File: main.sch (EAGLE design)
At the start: 49 parts, among them U2 SN65HVD32_D_8

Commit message: Organized Schematic
Added borders, boxes, and labels
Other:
- note added: "3.3V Switching Regulator"
- note added: "5V Tolerant Analog to Digital"
- note added: "BNO055 IMU"
- note added: "Designed around 100ohm output impedance pressure transducers"
- note added: "Digital IO Ports"
- note added: "Power Pins"
- note added: "RS-485 Tranceiver and Pins"
- note added: "SAMD21G18 Microcontroller"
- note added: "SWD Debuging Header"
- note added: "microSD card slot"
- note removed: "* MEANS UNFINISHED"
- note removed: "SAMD21G18"
- moved on the sheet: AIN, C1, C2, C23, C3, C4, C5, C6, C7, C8, C9, COM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

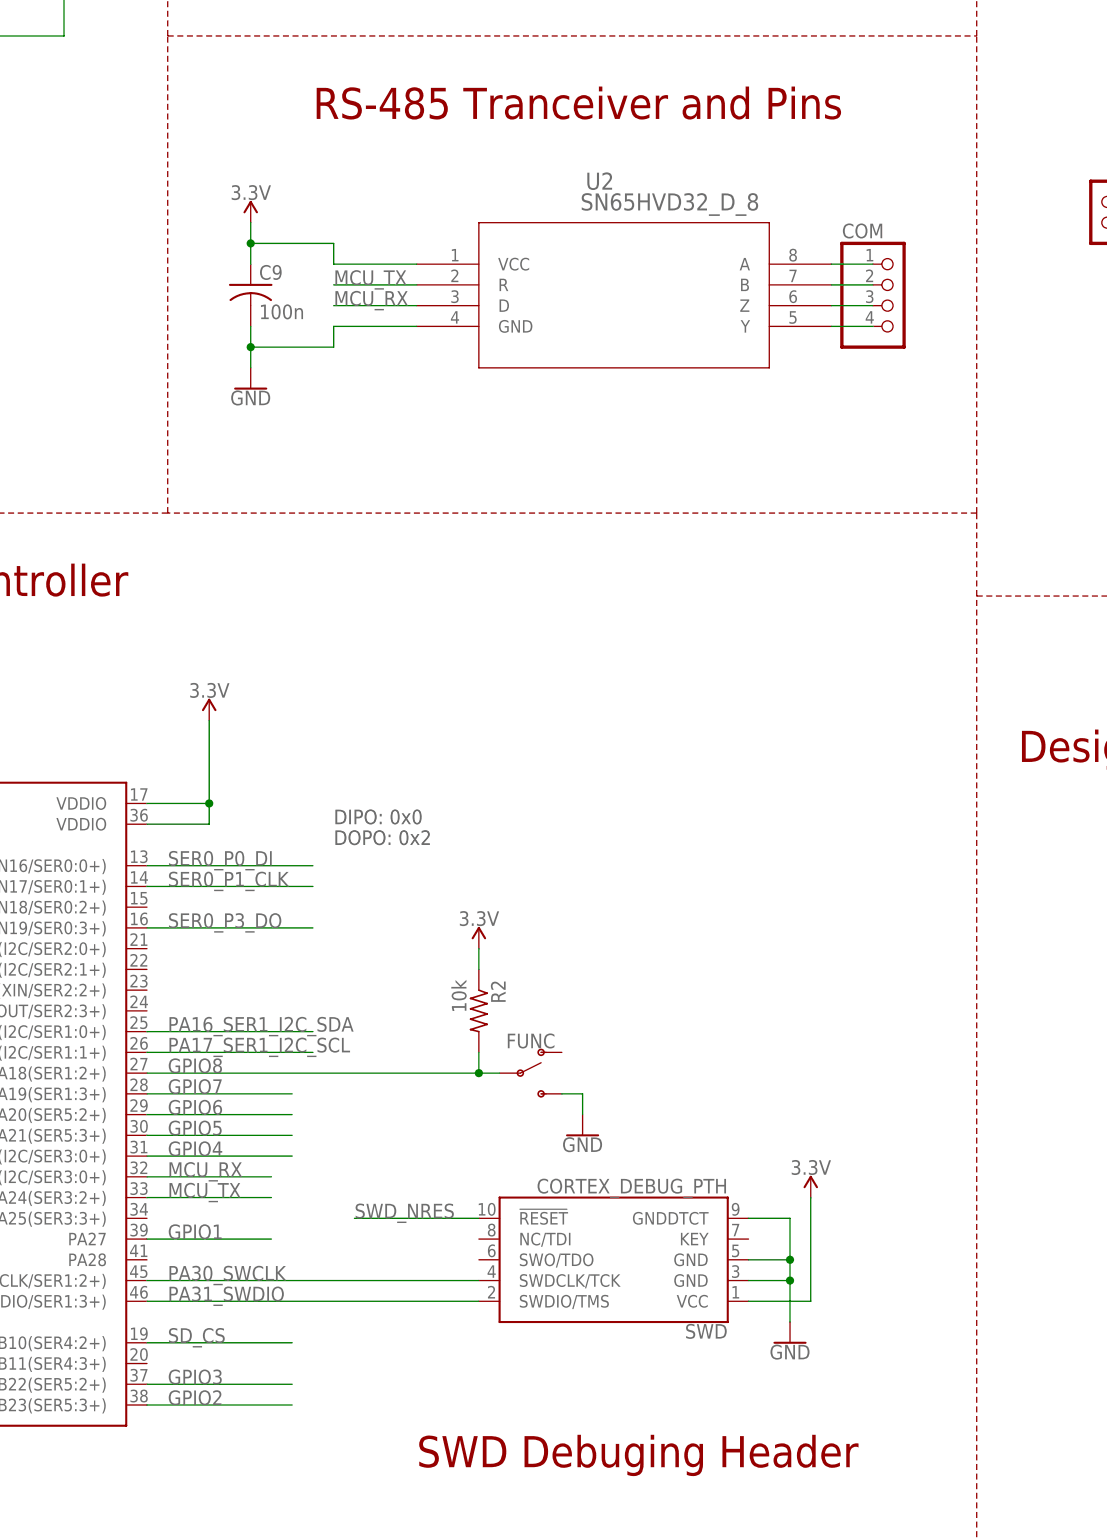
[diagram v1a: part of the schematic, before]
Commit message: Changed coms transceiver, and updated documentation
Also updated bill of materials
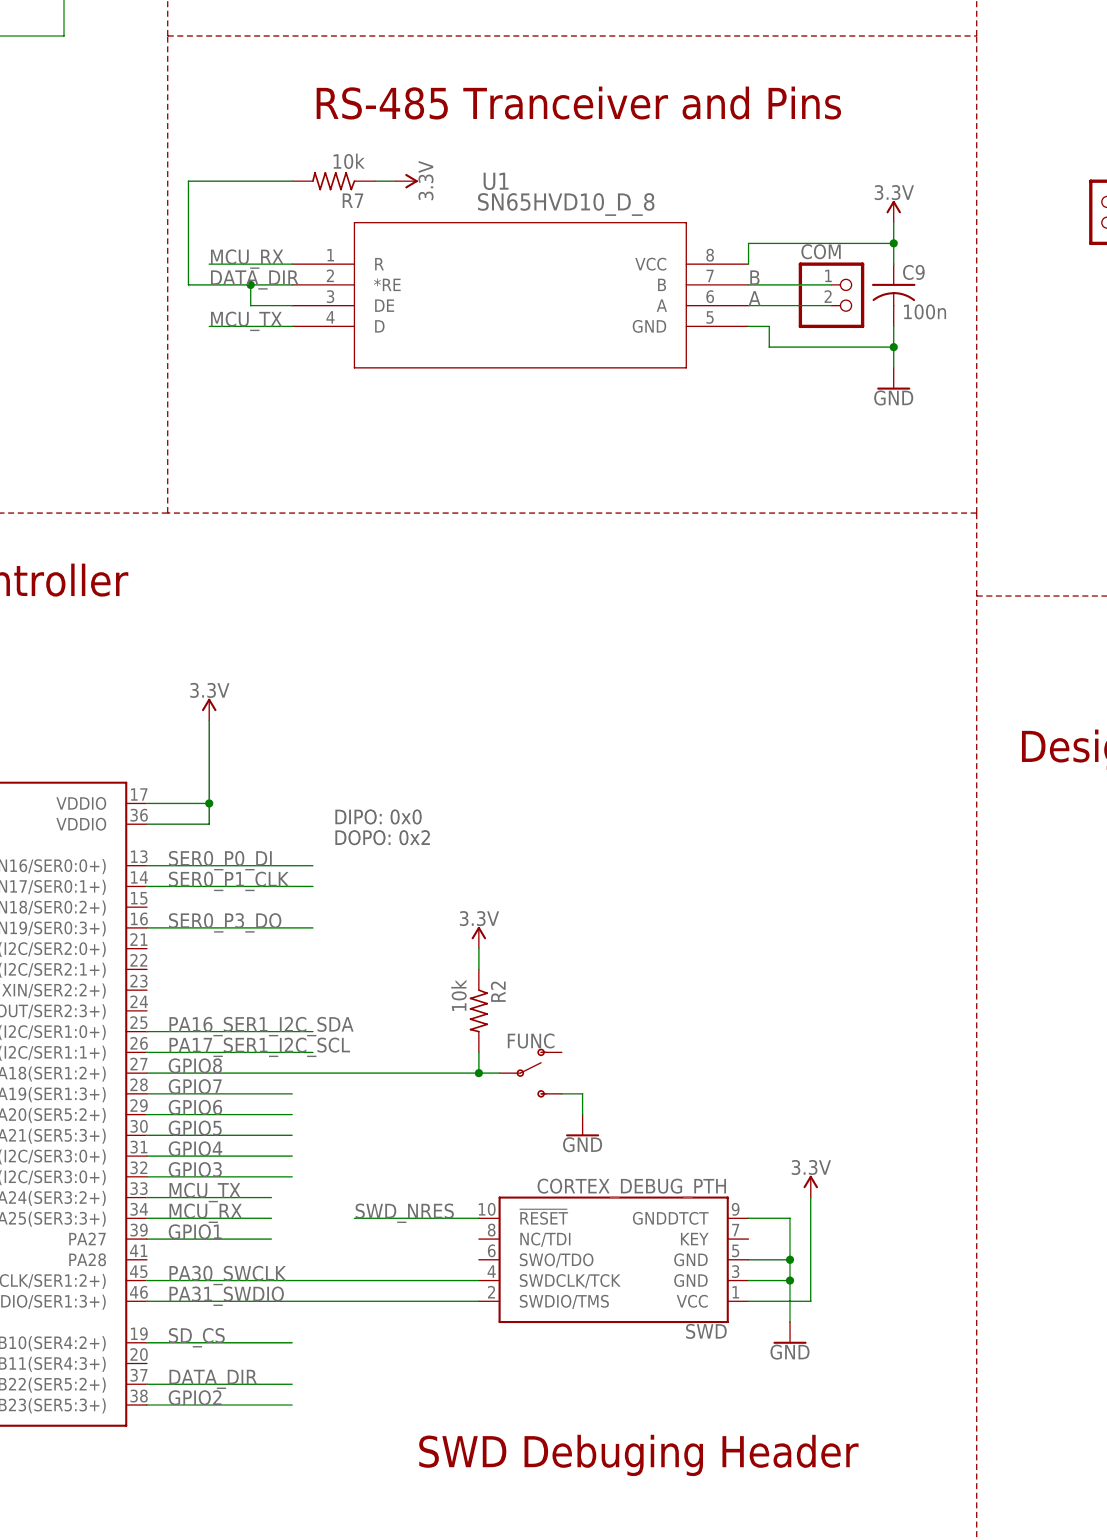
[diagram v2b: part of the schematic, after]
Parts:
- removed U2: SN65HVD32_D_8, SN65HVD32:SN65HVD32_D_8
- added R7: 10k, resistor:R-US_R0603
- added U1: SN65HVD10_D_8, half-dup-485:SN65HVD10_D_8
- COM: device pinhead:PINHD-1X4 -> pinhead:PINHD-1X2
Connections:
- removed net Y: COM.4, U2.Y
- removed net Z: COM.3, U2.Z
- new net DATA_DIR: MCU.PB22(SER5:2+), R7.2, U1.*RE, U1.DE
- net 3.3V: now also R7.1, U1.VCC; no longer U2.VCC
- net A: now also COM.2, U1.A; no longer COM.1, U2.A
- net B: now also COM.1, U1.B; no longer COM.2, U2.B
- net GND: now also U1.GND; no longer U2.GND
- net GPIO3: now also MCU.PA23(I2C/SER3:0+); no longer MCU.PB22(SER5:2+)
- net MCU_RX: now also MCU.PA25(SER3:3+), U1.R; no longer MCU.PA23(I2C/SER3:0+), U2.D
- net MCU_TX: now also U1.D; no longer U2.R
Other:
- moved on the sheet: C9
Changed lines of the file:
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@@
 <?xml version="1.0" encoding="utf-8"?>
 <!DOCTYPE eagle SYSTEM "eagle.dtd">
-<eagle version="8.6.3">
+<eagle version="8.6.0">
 <drawing>
 <settings>
@@
 <part name="SUPPLY16" library="SparkFun-PowerSymbols" deviceset="3.3V" device=""/>
 <part name="GND24" library="SparkFun-PowerSymbols" deviceset="GND" device=""/>
-<part name="U2" library="SN65HVD32" deviceset="SN65HVD32_D_8" device=""/>
-<part name="COM" library="pinhead" deviceset="PINHD-1X4" device=""/>
 <part name="AIN" library="pinhead" deviceset="PINHD-1X5" device=""/>
 <part name="VDUC" library="pinhead" deviceset="PINHD-1X2" device=""/>
@@
 <part name="PWR" library="SparkFun-Switches" deviceset="SWITCH-SPDT" device="-PTH-11.6X4.0MM"/>
 <part name="FRAME1" library="frames" library_urn="urn:adsk.eagle:library:229" deviceset="FRAME_B_L" device=""/>
+<part name="COM" library="pinhead" deviceset="PINHD-1X2" device=""/>
+<part name="U1" library="half-dup-485" deviceset="SN65HVD10_D_8" device=""/>
+<part name="R7" library="resistor" deviceset="R-US_" device="R0603" value="10k"/>
+<part name="SUPPLY13" library="SparkFun-PowerSymbols" deviceset="3.3V" device=""/>
 </parts>
 <sheets>
@@
 <instance part="R5" gate="G$1" x="76.2" y="109.22" rot="R270"/>
 <instance part="SUPPLY15" gate="G$1" x="76.2" y="116.84"/>
-<instance part="C9" gate="G$1" x="177.8" y="165.1"/>
-<instance part="SUPPLY16" gate="G$1" x="177.8" y="172.72"/>
-<instance part="GND24" gate="1" x="177.8" y="152.4"/>
-<instance part="U2" gate="A" x="198.12" y="167.64"/>
-<instance part="COM" gate="A" x="256.54" y="162.56"/>
+<instance part="C9" gate="G$1" x="256.54" y="165.1"/>
+<instance part="SUPPLY16" gate="G$1" x="256.54" y="172.72"/>
+<instance part="GND24" gate="1" x="256.54" y="152.4"/>
 <instance part="AIN" gate="A" x="393.7" y="91.44"/>
 <instance part="VDUC" gate="G$1" x="398.78" y="228.6"/>
@@
 <instance part="FRAME1" gate="G$1" x="0" y="0"/>
 <instance part="FRAME1" gate="G$2" x="325.12" y="0"/>
+<instance part="COM" gate="G$1" x="251.46" y="162.56"/>
+<instance part="U1" gate="A" x="182.88" y="167.64"/>
+<instance part="R7" gate="G$1" x="187.96" y="177.8" rot="R180"/>
+<instance part="SUPPLY13" gate="G$1" x="195.58" y="177.8" rot="R270"/>
 </instances>
 <busses>
@@
 <pinref part="C9" gate="G$1" pin="1"/>
 <pinref part="SUPPLY16" gate="G$1" pin="3.3V"/>
-<wire x1="177.8" y1="167.64" x2="177.8" y2="170.18" width="0.1524" layer="91"/>
-<pinref part="U2" gate="A" pin="VCC"/>
-<wire x1="177.8" y1="170.18" x2="177.8" y2="172.72" width="0.1524" layer="91"/>
-<wire x1="198.12" y1="167.64" x2="187.96" y2="167.64" width="0.1524" layer="91"/>
-<wire x1="187.96" y1="167.64" x2="187.96" y2="170.18" width="0.1524" layer="91"/>
-<wire x1="187.96" y1="170.18" x2="177.8" y2="170.18" width="0.1524" layer="91"/>
-<junction x="177.8" y="170.18"/>
+<wire x1="256.54" y1="167.64" x2="256.54" y2="170.18" width="0.1524" layer="91"/>
+<pinref part="U1" gate="A" pin="VCC"/>
+<wire x1="256.54" y1="170.18" x2="256.54" y2="172.72" width="0.1524" layer="91"/>
+<wire x1="238.76" y1="167.64" x2="238.76" y2="170.18" width="0.1524" layer="91"/>
+<wire x1="238.76" y1="170.18" x2="256.54" y2="170.18" width="0.1524" layer="91"/>
+<junction x="256.54" y="170.18"/>
 </segment>
 <segment>
@@
 <wire x1="205.74" y1="81.28" x2="205.74" y2="83.82" width="0.1524" layer="91"/>
 </segment>
+<segment>
+<pinref part="R7" gate="G$1" pin="1"/>
+<wire x1="193.04" y1="177.8" x2="195.58" y2="177.8" width="0.1524" layer="91"/>
+<pinref part="SUPPLY13" gate="G$1" pin="3.3V"/>
+</segment>
 </net>
 <net name="GND" class="0">
@@
 <pinref part="C9" gate="G$1" pin="2"/>
 <pinref part="GND24" gate="1" pin="GND"/>
-<wire x1="177.8" y1="154.94" x2="177.8" y2="157.48" width="0.1524" layer="91"/>
-<pinref part="U2" gate="A" pin="GND"/>
-<wire x1="177.8" y1="157.48" x2="177.8" y2="160.02" width="0.1524" layer="91"/>
-<wire x1="198.12" y1="160.02" x2="187.96" y2="160.02" width="0.1524" layer="91"/>
-<wire x1="187.96" y1="160.02" x2="187.96" y2="157.48" width="0.1524" layer="91"/>
-<wire x1="187.96" y1="157.48" x2="177.8" y2="157.48" width="0.1524" layer="91"/>
-<junction x="177.8" y="157.48"/>
+<wire x1="256.54" y1="154.94" x2="256.54" y2="157.48" width="0.1524" layer="91"/>
+<wire x1="256.54" y1="157.48" x2="256.54" y2="160.02" width="0.1524" layer="91"/>
+<wire x1="256.54" y1="157.48" x2="241.3" y2="157.48" width="0.1524" layer="91"/>
+<wire x1="241.3" y1="157.48" x2="241.3" y2="160.02" width="0.1524" layer="91"/>
+<junction x="256.54" y="157.48"/>
+<pinref part="U1" gate="A" pin="GND"/>
+<wire x1="241.3" y1="160.02" x2="238.76" y2="160.02" width="0.1524" layer="91"/>
 </segment>
 <segment>
@@
 <net name="MCU_TX" class="0">
 <segment>
-<pinref part="U2" gate="A" pin="R"/>
-<wire x1="198.12" y1="165.1" x2="187.96" y2="165.1" width="0.1524" layer="91"/>
-<label x="187.96" y="165.1" size="1.778" layer="95"/>
-</segment>
-<segment>
 <pinref part="MCU" gate="G$1" pin="PA24(SER3:2+)"/>
 <wire x1="165.1" y1="53.34" x2="180.34" y2="53.34" width="0.1524" layer="91"/>
 <label x="167.64" y="53.34" size="1.778" layer="95"/>
 </segment>
+<segment>
+<wire x1="182.88" y1="160.02" x2="172.72" y2="160.02" width="0.1524" layer="91"/>
+<label x="172.72" y="160.02" size="1.778" layer="95"/>
+<pinref part="U1" gate="A" pin="D"/>
+</segment>
 </net>
 <net name="MCU_RX" class="0">
 <segment>
-<pinref part="U2" gate="A" pin="D"/>
-<wire x1="198.12" y1="162.56" x2="187.96" y2="162.56" width="0.1524" layer="91"/>
-<label x="187.96" y="162.56" size="1.778" layer="95"/>
-</segment>
-<segment>
-<pinref part="MCU" gate="G$1" pin="PA23(I2C/SER3:0+)"/>
-<wire x1="165.1" y1="55.88" x2="180.34" y2="55.88" width="0.1524" layer="91"/>
-<label x="167.64" y="55.88" size="1.778" layer="95"/>
-</segment>
-</net>
-<net name="A" class="0">
-<segment>
-<pinref part="U2" gate="A" pin="A"/>
-<pinref part="COM" gate="A" pin="1"/>
-<wire x1="248.92" y1="167.64" x2="254" y2="167.64" width="0.1524" layer="91"/>
-</segment>
-</net>
-<net name="B" class="0">
-<segment>
-<pinref part="U2" gate="A" pin="B"/>
-<pinref part="COM" gate="A" pin="2"/>
-<wire x1="248.92" y1="165.1" x2="254" y2="165.1" width="0.1524" layer="91"/>
-</segment>
-</net>
-<net name="Z" class="0">
-<segment>
-<pinref part="U2" gate="A" pin="Z"/>
-<pinref part="COM" gate="A" pin="3"/>
-<wire x1="248.92" y1="162.56" x2="254" y2="162.56" width="0.1524" layer="91"/>
-</segment>
-</net>
-<net name="Y" class="0">
-<segment>
-<pinref part="U2" gate="A" pin="Y"/>
-<pinref part="COM" gate="A" pin="4"/>
-<wire x1="248.92" y1="160.02" x2="254" y2="160.02" width="0.1524" layer="91"/>
+<wire x1="182.88" y1="167.64" x2="172.72" y2="167.64" width="0.1524" layer="91"/>
+<label x="172.72" y="167.64" size="1.778" layer="95"/>
+<pinref part="U1" gate="A" pin="R"/>
+</segment>
+<segment>
+<pinref part="MCU" gate="G$1" pin="PA25(SER3:3+)"/>
+<wire x1="165.1" y1="50.8" x2="180.34" y2="50.8" width="0.1524" layer="91"/>
+<label x="167.64" y="50.8" size="1.778" layer="95"/>
 </segment>
 </net>
@@
 </segment>
 <segment>
-<pinref part="MCU" gate="G$1" pin="PB22(SER5:2+)"/>
-<wire x1="165.1" y1="30.48" x2="182.88" y2="30.48" width="0.1524" layer="91"/>
-<label x="167.64" y="30.48" size="1.778" layer="95"/>
+<pinref part="MCU" gate="G$1" pin="PA23(I2C/SER3:0+)"/>
+<wire x1="165.1" y1="55.88" x2="182.88" y2="55.88" width="0.1524" layer="91"/>
+<label x="167.64" y="55.88" size="1.778" layer="95"/>
 </segment>
 </net>
@@
 </segment>
 </net>
+<net name="DATA_DIR" class="0">
+<segment>
+<pinref part="U1" gate="A" pin="DE"/>
+<wire x1="182.88" y1="162.56" x2="177.8" y2="162.56" width="0.1524" layer="91"/>
+<wire x1="177.8" y1="162.56" x2="177.8" y2="165.1" width="0.1524" layer="91"/>
+<pinref part="U1" gate="A" pin="*RE"/>
+<wire x1="177.8" y1="165.1" x2="182.88" y2="165.1" width="0.1524" layer="91"/>
+<wire x1="177.8" y1="165.1" x2="170.18" y2="165.1" width="0.1524" layer="91"/>
+<junction x="177.8" y="165.1"/>
+<label x="172.72" y="165.1" size="1.778" layer="95"/>
+<wire x1="170.18" y1="165.1" x2="170.18" y2="177.8" width="0.1524" layer="91"/>
+<wire x1="170.18" y1="177.8" x2="182.88" y2="177.8" width="0.1524" layer="91"/>
+<pinref part="R7" gate="G$1" pin="2"/>
+</segment>
+<segment>
+<pinref part="MCU" gate="G$1" pin="PB22(SER5:2+)"/>
+<wire x1="165.1" y1="30.48" x2="182.88" y2="30.48" width="0.1524" layer="91"/>
+<label x="167.64" y="30.48" size="1.778" layer="95"/>
+</segment>
+</net>
+<net name="B" class="0">
+<segment>
+<pinref part="COM" gate="G$1" pin="1"/>
+<pinref part="U1" gate="A" pin="B"/>
+<wire x1="248.92" y1="165.1" x2="238.76" y2="165.1" width="0.1524" layer="91"/>
+<label x="238.76" y="165.1" size="1.778" layer="95"/>
+</segment>
+</net>
+<net name="A" class="0">
+<segment>
+<pinref part="COM" gate="G$1" pin="2"/>
+<pinref part="U1" gate="A" pin="A"/>
+<wire x1="248.92" y1="162.56" x2="238.76" y2="162.56" width="0.1524" layer="91"/>
+<label x="238.76" y="162.56" size="1.778" layer="95"/>
+</segment>
+</net>
